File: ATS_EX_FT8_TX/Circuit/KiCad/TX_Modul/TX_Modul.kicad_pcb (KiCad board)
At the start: 2 copper layers, 16 parts, among them J1 Conn_01x15_Socket, J2 Conn_01x15_Socket, J3 From PC, J4 Relais, J5 Conn_01x02_Socket, J6 Conn_01x06_Socket, J7 Conn_01x06_Socket, J8 Conn_01x06_Socket

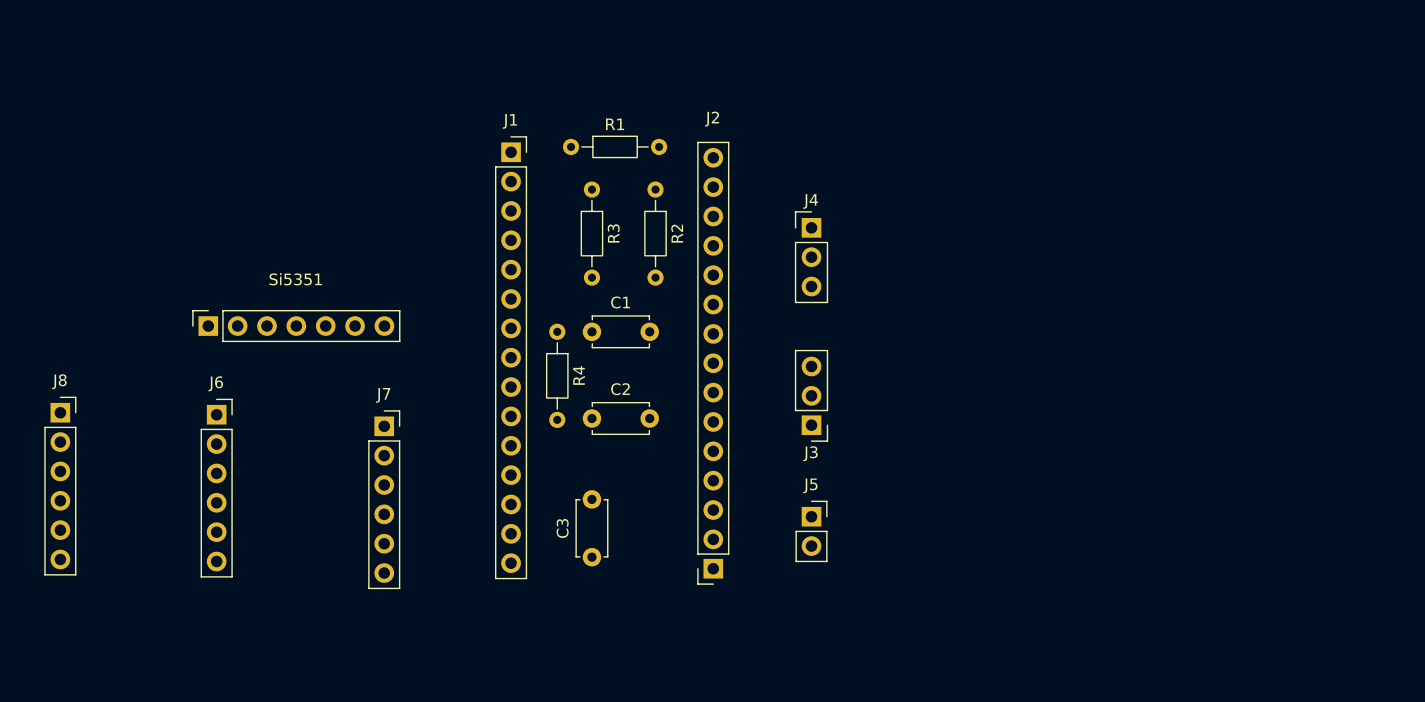
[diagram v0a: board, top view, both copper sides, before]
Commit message: update KiCad TX Module
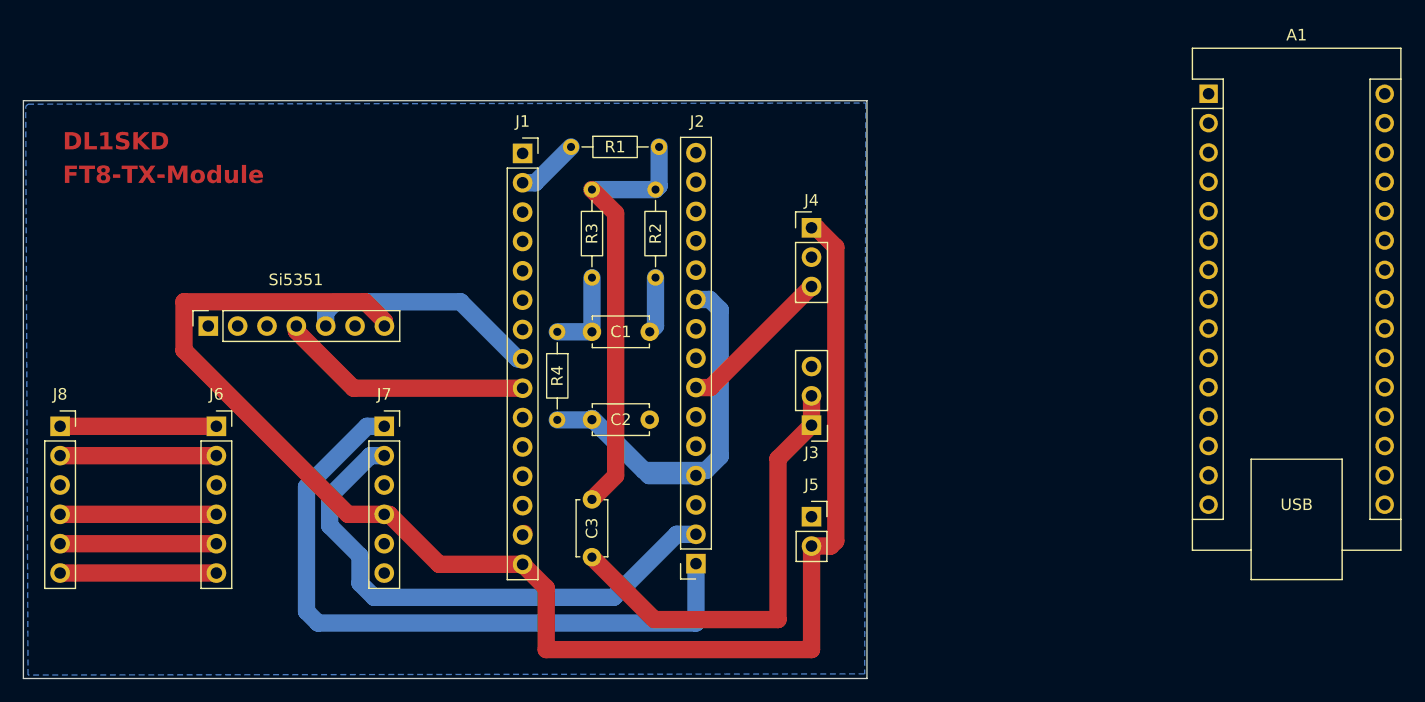
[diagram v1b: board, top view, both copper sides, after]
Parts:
- added A1: Arduino_Nano_v3.x, Module:Arduino_Nano, F.Cu at (215.9, 34.4)
- moved J2 1.56 mm to (171.5, 75.1)
- moved J8 1.18 mm to (116.5, 63.2)
- moved J1 1.00 mm to (156.5, 39.6)
- moved J6 1.00 mm to (130.0, 63.2)
- moved C2 0.10 mm to (162.5, 62.6)
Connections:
- J1 pad 14: Net-(J1-Pin_14) -> GND
- J5 pad 1: Net-(J1-Pin_14) -> GND
- J6 pad 3: Net-(J6-Pin_3) -> GND
- J7 pad 3: Net-(J1-Pin_14) -> GND
- J8 pad 3: Net-(J6-Pin_3) -> GND
- Si5351 pad 6: Net-(J1-Pin_14) -> GND
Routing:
- net Net-(J1-Pin_15): track 0.00 -> 130.3 mm
- net Net-(J2-Pin_1): track 0.00 -> 58.9 mm
- net Net-(J2-Pin_2): track 0.00 -> 46.6 mm
- net Net-(C2-+): track 0.00 -> 42.7 mm
- net Net-(C3-+): track 0.00 -> 38.9 mm
- net Net-(C3--): track 0.00 -> 37.8 mm
- net Net-(J1-Pin_9): track 0.00 -> 22.1 mm
- net Net-(J1-Pin_8): track 0.00 -> 20.7 mm
- net Net-(J2-Pin_7): track 0.00 -> 13.6 mm
- net Net-(J6-Pin_6): track 0.00 -> 13.5 mm
- net Net-(J6-Pin_5): track 0.00 -> 13.5 mm
- net Net-(J6-Pin_4): track 0.00 -> 13.5 mm
- net Net-(J6-Pin_2): track 0.00 -> 13.5 mm
- net Net-(J6-Pin_1): track 0.00 -> 13.5 mm
- net Net-(C1-+): track 0.00 -> 7.69 mm
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- added copper zone on B.Cu, net GND
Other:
- board outline added: 73 x 50 mm
- board text added: "DL1SKD"
- board text added: "FT8-TX-Module"

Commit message: Update Platine
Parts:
- added Si1: Conn_01x07_Socket, Connector_PinSocket_2.54mm:PinSocket_1x07_P2.54mm_Vertical, F.Cu at (129.3, 44.6)
- moved A1 6.97 mm to (209.0, 35.4)
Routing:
- net Net-(C2-+): track 42.7 -> 30.6 mm
- net Net-(J1-Pin_15): track 130.3 -> 119.3 mm
- net Net-(C3-+): track 38.9 -> 30.8 mm
- net GND: track 5.08 -> 0.89 mm
- net Net-(J2-Pin_1): track 58.9 -> 55.4 mm
- net Net-(J1-Pin_8): track 20.7 -> 18.6 mm
- net Net-(J2-Pin_2): track 46.6 -> 47.9 mm
- net Net-(C3--): track 37.8 -> 37.3 mm
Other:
- board text added: "+"
- board text added: "-"
- board text added: "L"
- board text added: "Levelshifter"
- board text added: "R"
- board text added: "S"

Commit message: Update TX PCB
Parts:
- added H1: MountingHole_M3, MountingHole:MountingHole_3.2mm_M3, F.Cu at (117.5, 39.0)
- added H2: MountingHole_M3, MountingHole:MountingHole_3.2mm_M3, F.Cu at (117.5, 81.0)
- added H3: MountingHole_M3, MountingHole:MountingHole_3.2mm_M3, F.Cu at (182.5, 39.0)
- added H4: MountingHole_M3, MountingHole:MountingHole_3.2mm_M3, F.Cu at (182.5, 81.0)
- moved J6 4.06 mm to (134.0, 62.5)
- moved J8 1.67 mm to (118.0, 62.5)
- moved J7 0.67 mm to (144.5, 62.5)
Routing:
- net Net-(J1-Pin_15): track 119.3 -> 131.9 mm
- net Net-(J6-Pin_6): track 13.5 -> 16.0 mm
- net Net-(J6-Pin_5): track 13.5 -> 16.0 mm
- net Net-(J6-Pin_4): track 13.5 -> 16.0 mm
- net Net-(J6-Pin_2): track 13.5 -> 16.0 mm
- net Net-(J6-Pin_1): track 13.5 -> 16.0 mm
- removed copper zone on B.Cu, net GND

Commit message: Update Schematic
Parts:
- renumbered J5 to 5V1
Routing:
- added copper zone on B.Cu, net GND

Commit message: Gerber
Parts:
- removed A1: Arduino_Nano_v3.x, Module:Arduino_Nano
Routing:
- net Net-(J2-Pin_1): track 55.4 -> 56.7 mm
- net Net-(J2-Pin_2): track 47.9 -> 48.8 mm
